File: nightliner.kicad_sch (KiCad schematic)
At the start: 81 parts, among them J1 TYPE-C-31-M-12, J2 Battery, J3 Battery, SW1 SW_SPST, SW10 SW_SPST, SW11 SW_SPST, SW12 SW_SPST, SW13 SW_SPST, SW14 SW_SPST, SW15 SW_SPST, SW16 SW_SPST, SW17 SW_SPST, SW18 SW_SPST, SW19 SW_SPST, SW2 SW_SPST, SW20 SW_SPST, SW21 ON_OFF, SW22 RESET, SW3 SW_SPST, SW4 SW_SPST, SW5 SW_SPST, SW6 SW_SPST, SW7 SW_SPST, SW8 SW_SPST, SW9 SW_SPST, U1 holyiot-18010, U2 TVS2200DRV, U3 USBLC6-2SC6, U4 BQ24075RGT, U5 XC6220B331MR

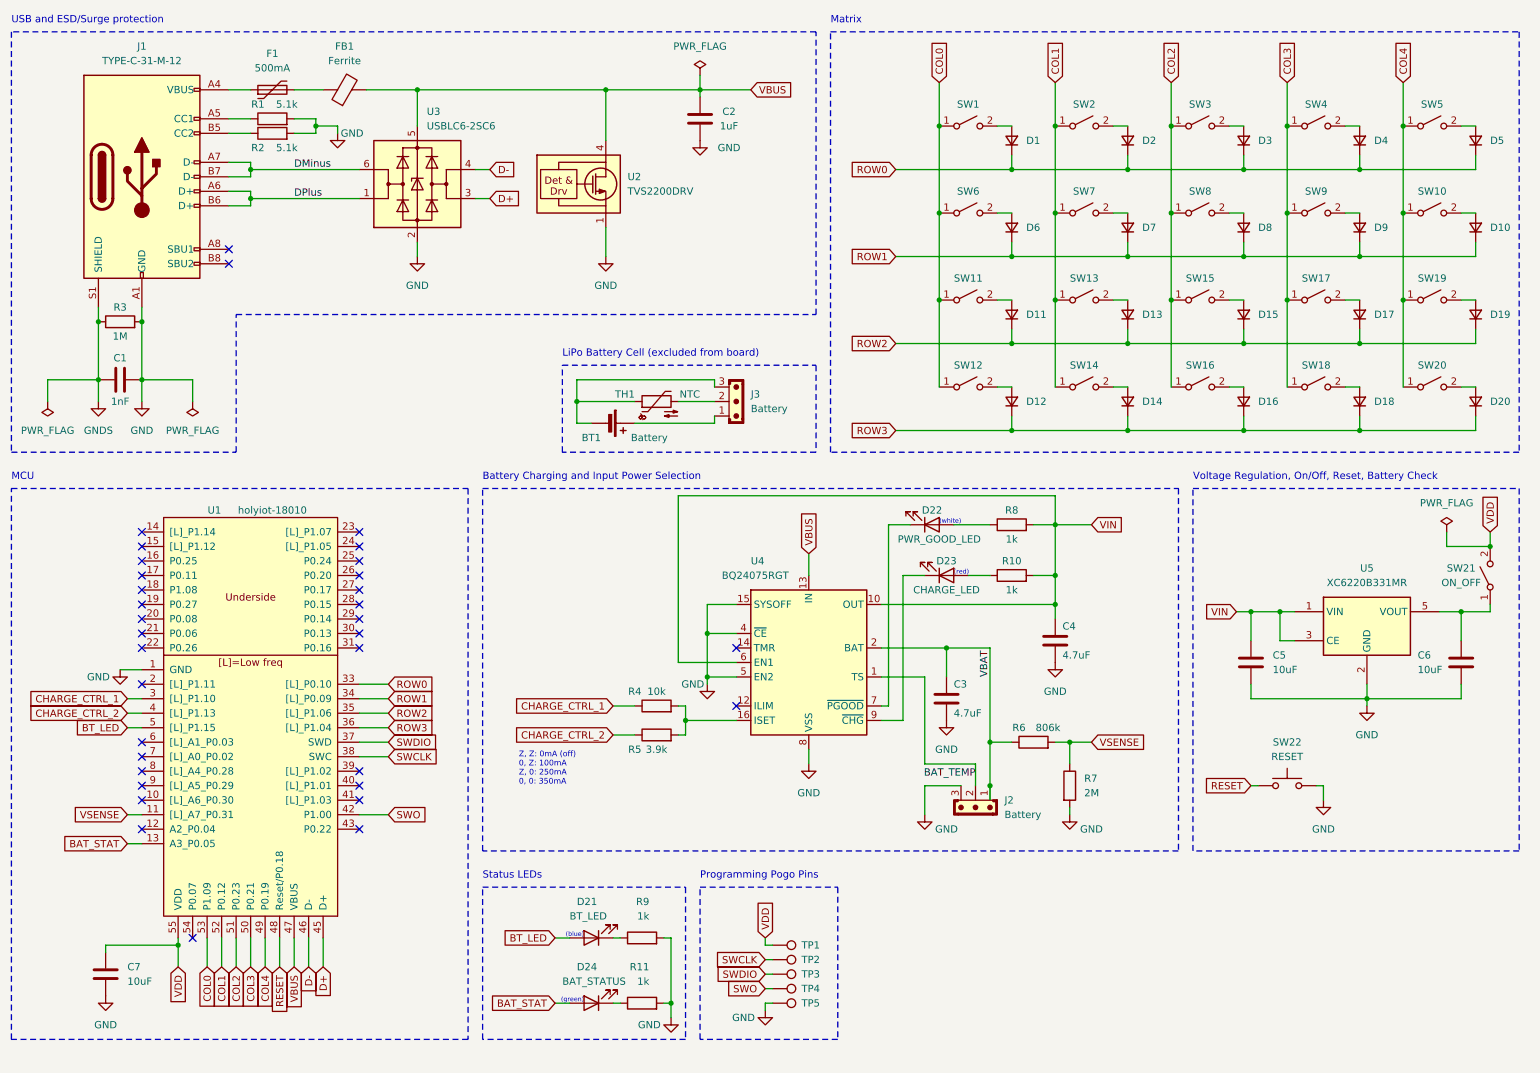
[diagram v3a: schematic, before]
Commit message: feat: routed PCB, ready for fills
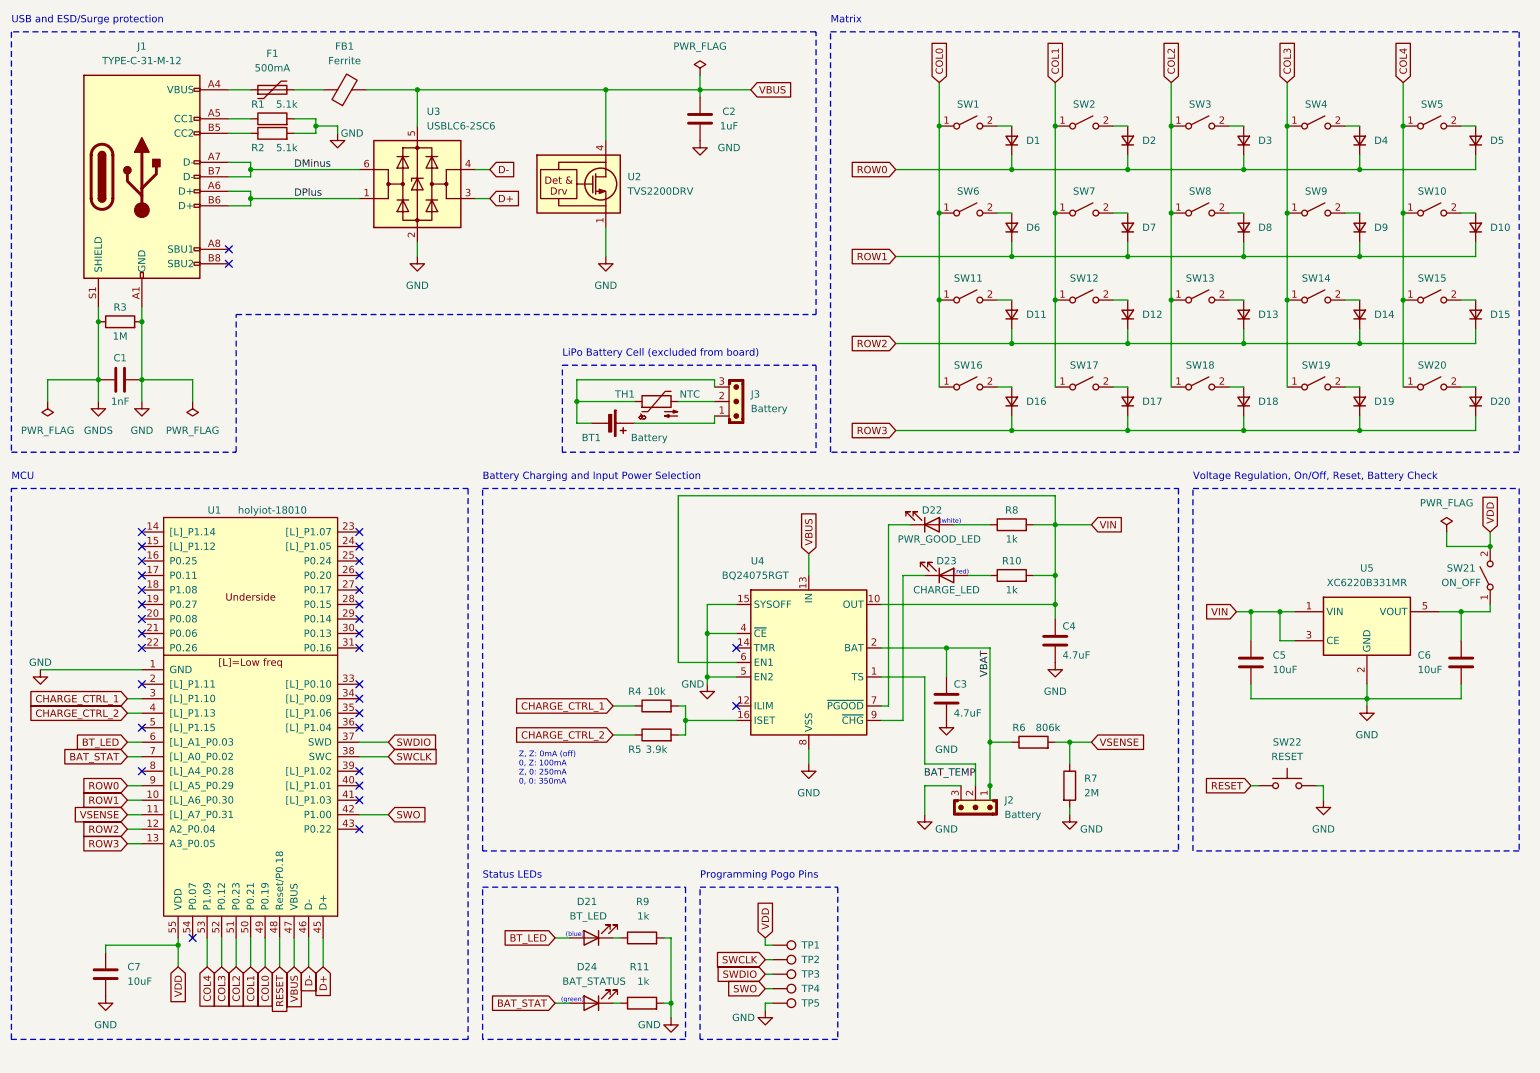
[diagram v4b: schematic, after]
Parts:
- SW1: value SW_SPST -> pinky_top
- SW10: value SW_SPST -> inner_home
- SW11: value SW_SPST -> pinky_bottom
- SW12: renamed from SW13; value SW_SPST -> ring_bottom
- SW13: renamed from SW15; value SW_SPST -> middle_bottom
- SW14: renamed from SW17; value SW_SPST -> index_bottom
- SW15: renamed from SW19; value SW_SPST -> inner_bottom
- SW16: renamed from SW12; value SW_SPST -> outer_top
- SW17: renamed from SW14; value SW_SPST -> outer_home
- SW18: renamed from SW16; value SW_SPST -> near_thumb
- SW19: renamed from SW18; value SW_SPST -> home_thumb
- SW2: value SW_SPST -> ring_top
- SW20: value SW_SPST -> far_thumb
- SW3: value SW_SPST -> middle_top
- SW4: value SW_SPST -> index_top
- SW5: value SW_SPST -> inner_top
- SW6: value SW_SPST -> pinky_home
- SW7: value SW_SPST -> ring_home
- SW8: value SW_SPST -> middle_home
- SW9: value SW_SPST -> index_home
- renumbered D13 to D12, D15 to D13, D17 to D14, D19 to D15, D12 to D16, D14 to D17, D16 to D18, D18 to D19
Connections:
- net BAT_STAT: now also U1.7 ([L]_A0_P0.02); no longer U1.13 (A3_P0.05)
- net BT_LED: now also U1.6 ([L]_A1_P0.03); no longer U1.5 ([L]_P1.15)
- net COL0: now also U1.49 (P0.19); no longer U1.53 (P1.09)
- net COL1: now also U1.50 (P0.21); no longer U1.52 (P0.12)
- net COL3: now also U1.52 (P0.12); no longer U1.50 (P0.21)
- net COL4: now also U1.53 (P1.09); no longer U1.49 (P0.19)
- net ROW0: now also U1.9 ([L]_A5_P0.29); no longer U1.33 ([L]_P0.10)
- net ROW1: now also U1.10 ([L]_A6_P0.30); no longer U1.34 ([L]_P0.09)
- net ROW2: now also U1.12 (A2_P0.04); no longer U1.35 ([L]_P1.06)
- net ROW3: now also U1.13 (A3_P0.05); no longer U1.36 ([L]_P1.04)

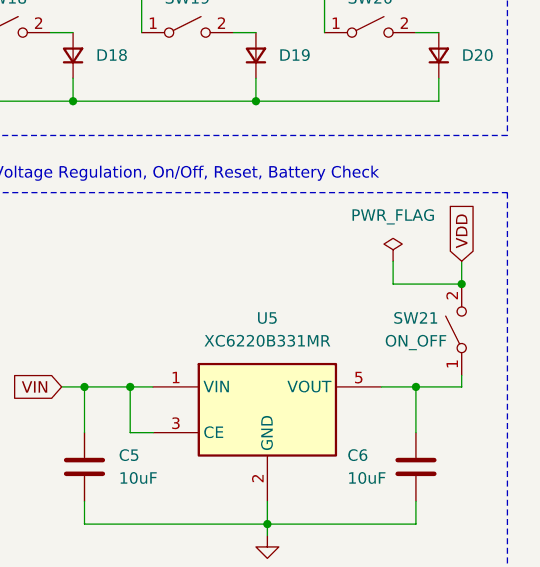
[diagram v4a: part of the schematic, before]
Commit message: fix: DRC errors, updated footprints
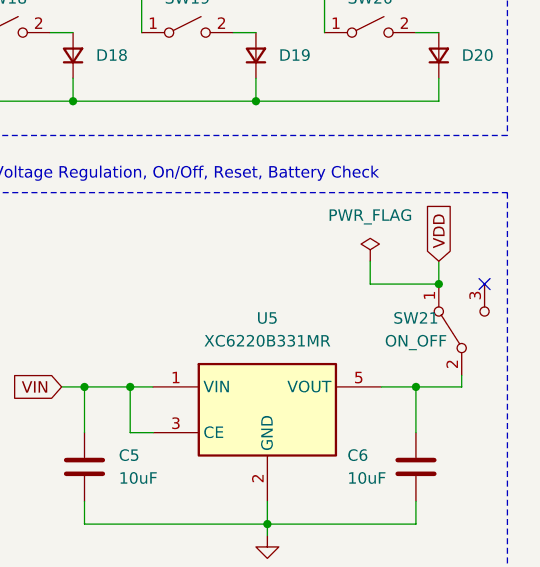
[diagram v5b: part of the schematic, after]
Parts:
- D1, D10, D11, D12, D13, D14, D15, D16, D17, D18, D19, D2, D20, D3, D4, D5, D6, D7, D8, D9: footprint keebio:D_SOD-323 -> Diode_SMD:D_SOD-323
- SW21: symbol Switch:SW_SPST -> Switch:SW_SPDT
- U4: footprint Package_DFN_QFN:VQFN-16-1EP_3x3mm_P0.5mm_EP1.6x1.6mm -> miro_keyboard:VQFN-16-1EP_3x3mm_P0.5mm_EP1.6x1.6mm_ThermalVias
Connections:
- net VDD: now also SW21.1 (A); no longer SW21.2 (B)
- net at C6.1, U5.5 (VOUT): now also SW21.2 (B); no longer SW21.1 (A)
- no-connect marks 34 -> 35
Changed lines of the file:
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@@
   (junction (at 252.73 72.39) (diameter 0) (color 0 0 0 0)
   )
-  (junction (at 275.59 107.95) (diameter 0) (color 0 0 0 0)
-  )
   (junction (at 31.75 78.74) (diameter 0) (color 0 0 0 0)
   )
@@
   (junction (at 179.07 64.77) (diameter 0) (color 0 0 0 0)
   )
+  (junction (at 273.05 107.95) (diameter 0) (color 0 0 0 0)
+  )
   (junction (at 212.09 72.39) (diameter 0) (color 0 0 0 0)
   )
@@
   (no_connect (at 77.47 118.11))
   (no_connect (at 77.47 115.57))
+  (no_connect (at 278.13 107.95))
   (no_connect (at 39.37 118.11))
   (no_connect (at 39.37 115.57))
@@
     (stroke (width 0) (type default))
   )
-  (wire (pts (xy 275.59 105.41) (xy 275.59 107.95))
+  (wire (pts (xy 273.05 105.41) (xy 273.05 107.95))
     (stroke (width 0) (type default))
   )
@@
     (stroke (width 0) (type default))
   )
-  (wire (pts (xy 267.97 107.95) (xy 275.59 107.95))
+  (wire (pts (xy 265.43 107.95) (xy 273.05 107.95))
     (stroke (width 0) (type default))
   )
@@
     (stroke (width 0) (type default))
   )
-  (wire (pts (xy 267.97 105.41) (xy 267.97 107.95))
+  (wire (pts (xy 265.43 105.41) (xy 265.43 107.95))
     (stroke (width 0) (type default))
   )
@@
     )
   )
-  (global_label "VDD" (shape input) (at 275.59 105.41 90) (fields_autoplaced)
+  (global_label "VDD" (shape input) (at 273.05 105.41 90) (fields_autoplaced)
     (effects (font (size 1.27 1.27)) (justify left))
-    (property "Intersheetrefs" "${INTERSHEET_REFS}" (at 275.59 98.7962 90)
+    (property "Intersheetrefs" "${INTERSHEET_REFS}" (at 273.05 98.7962 90)
       (effects (font (size 1.27 1.27)) (justify left) hide)
     )
@@
       (effects (font (size 1.27 1.27)) (justify right) hide)
     )
-    (property "Footprint" "keebio:D_SOD-323" (at 212.09 52.07 90)
+    (property "Footprint" "Diode_SMD:D_SOD-323" (at 212.09 52.07 90)
       (effects (font (size 1.27 1.27)) hide)
     )
@@
       (effects (font (size 1.27 1.27)) (justify right) hide)
     )
-    (property "Footprint" "keebio:D_SOD-323" (at 273.05 36.83 90)
+    (property "Footprint" "Diode_SMD:D_SOD-323" (at 273.05 36.83 90)
       (effects (font (size 1.27 1.27)) hide)
     )
@@
       (effects (font (size 1.27 1.27)) (justify right) hide)
     )
-    (property "Footprint" "keebio:D_SOD-323" (at 212.09 67.31 90)
+    (property "Footprint" "Diode_SMD:D_SOD-323" (at 212.09 67.31 90)
       (effects (font (size 1.27 1.27)) hide)
     )
@@
       (effects (font (size 1.27 1.27)) (justify right) hide)
     )
-    (property "Footprint" "keebio:D_SOD-323" (at 252.73 52.07 90)
+    (property "Footprint" "Diode_SMD:D_SOD-323" (at 252.73 52.07 90)
       (effects (font (size 1.27 1.27)) hide)
     )
@@
     )
   )
-  (symbol (lib_id "Switch:SW_SPST") (at 275.59 113.03 90) (unit 1)
+  (symbol (lib_id "Switch:SW_SPDT") (at 275.59 113.03 90) (unit 1)
     (in_bom yes) (on_board yes) (dnp no)
     (property "Reference" "SW21" (at 270.51 111.76 90)
@@
     (pin "1")
     (pin "2")
+    (pin "3")
     (instances
       (project "nightliner"
@@
     )
   )
-  (symbol (lib_id "power:PWR_FLAG") (at 267.97 105.41 0) (unit 1)
+  (symbol (lib_id "power:PWR_FLAG") (at 265.43 105.41 0) (unit 1)
     (in_bom yes) (on_board yes) (dnp no) (fields_autoplaced)
-    (property "Reference" "#FLG03" (at 267.97 103.505 0)
+    (property "Reference" "#FLG03" (at 265.43 103.505 0)
       (effects (font (size 1.27 1.27)) hide)
     )
-    (property "Value" "PWR_FLAG" (at 267.97 100.33 0)
+    (property "Value" "PWR_FLAG" (at 265.43 100.33 0)
       (effects (font (size 1.27 1.27)))
     )
-    (property "Footprint" "" (at 267.97 105.41 0)
+    (property "Footprint" "" (at 265.43 105.41 0)
       (effects (font (size 1.27 1.27)) hide)
     )
-    (property "Datasheet" "~" (at 267.97 105.41 0)
+    (property "Datasheet" "~" (at 265.43 105.41 0)
       (effects (font (size 1.27 1.27)) hide)
     )
@@
       (effects (font (size 1.27 1.27)) (justify right) hide)
     )
-    (property "Footprint" "keebio:D_SOD-323" (at 191.77 36.83 90)
+    (property "Footprint" "Diode_SMD:D_SOD-323" (at 191.77 36.83 90)
       (effects (font (size 1.27 1.27)) hide)
     )
@@
       (effects (font (size 1.27 1.27)) (justify right) hide)
     )
-    (property "Footprint" "keebio:D_SOD-323" (at 232.41 52.07 90)
+    (property "Footprint" "Diode_SMD:D_SOD-323" (at 232.41 52.07 90)
       (effects (font (size 1.27 1.27)) hide)
     )
@@
       (effects (font (size 1.27 1.27)) (justify right) hide)
     )
-    (property "Footprint" "keebio:D_SOD-323" (at 273.05 67.31 90)
+    (property "Footprint" "Diode_SMD:D_SOD-323" (at 273.05 67.31 90)
       (effects (font (size 1.27 1.27)) hide)
     )
@@
       (effects (font (size 1.27 1.27)) (justify right) hide)
     )
-    (property "Footprint" "keebio:D_SOD-323" (at 232.41 82.55 90)
+    (property "Footprint" "Diode_SMD:D_SOD-323" (at 232.41 82.55 90)
       (effects (font (size 1.27 1.27)) hide)
     )
@@
       (effects (font (size 1.27 1.27)) (justify right) hide)
     )
-    (property "Footprint" "keebio:D_SOD-323" (at 273.05 82.55 90)
+    (property "Footprint" "Diode_SMD:D_SOD-323" (at 273.05 82.55 90)
       (effects (font (size 1.27 1.27)) hide)
     )
@@
       (effects (font (size 1.27 1.27)) (justify right) hide)
     )
-    (property "Footprint" "keebio:D_SOD-323" (at 252.73 36.83 90)
+    (property "Footprint" "Diode_SMD:D_SOD-323" (at 252.73 36.83 90)
       (effects (font (size 1.27 1.27)) hide)
     )
@@
       (effects (font (size 1.27 1.27)) (justify right) hide)
     )
-    (property "Footprint" "keebio:D_SOD-323" (at 191.77 82.55 90)
+    (property "Footprint" "Diode_SMD:D_SOD-323" (at 191.77 82.55 90)
       (effects (font (size 1.27 1.27)) hide)
     )
@@
       (effects (font (size 1.27 1.27)) (justify right) hide)
     )
-    (property "Footprint" "keebio:D_SOD-323" (at 273.05 52.07 90)
+    (property "Footprint" "Diode_SMD:D_SOD-323" (at 273.05 52.07 90)
       (effects (font (size 1.27 1.27)) hide)
     )
@@
       (effects (font (size 1.27 1.27)) (justify right) hide)
     )
-    (property "Footprint" "keebio:D_SOD-323" (at 191.77 52.07 90)
+    (property "Footprint" "Diode_SMD:D_SOD-323" (at 191.77 52.07 90)
       (effects (font (size 1.27 1.27)) hide)
     )
@@
       (effects (font (size 1.27 1.27)) (justify right) hide)
     )
-    (property "Footprint" "keebio:D_SOD-323" (at 191.77 67.31 90)
+    (property "Footprint" "Diode_SMD:D_SOD-323" (at 191.77 67.31 90)
       (effects (font (size 1.27 1.27)) hide)
     )
@@
       (effects (font (size 1.27 1.27)) (justify right) hide)
     )
-    (property "Footprint" "keebio:D_SOD-323" (at 232.41 36.83 90)
+    (property "Footprint" "Diode_SMD:D_SOD-323" (at 232.41 36.83 90)
       (effects (font (size 1.27 1.27)) hide)
     )
@@
       (effects (font (size 1.27 1.27)) (justify right) hide)
     )
-    (property "Footprint" "keebio:D_SOD-323" (at 212.09 82.55 90)
+    (property "Footprint" "Diode_SMD:D_SOD-323" (at 212.09 82.55 90)
       (effects (font (size 1.27 1.27)) hide)
     )
@@
       (effects (font (size 1.27 1.27)) (justify right) hide)
     )
-    (property "Footprint" "keebio:D_SOD-323" (at 252.73 82.55 90)
+    (property "Footprint" "Diode_SMD:D_SOD-323" (at 252.73 82.55 90)
       (effects (font (size 1.27 1.27)) hide)
     )
@@
       (effects (font (size 1.27 1.27)) (justify right) hide)
     )
-    (property "Footprint" "keebio:D_SOD-323" (at 252.73 67.31 90)
+    (property "Footprint" "Diode_SMD:D_SOD-323" (at 252.73 67.31 90)
       (effects (font (size 1.27 1.27)) hide)
     )
@@
       (effects (font (size 1.27 1.27)) (justify left))
     )
-    (property "Footprint" "Package_DFN_QFN:VQFN-16-1EP_3x3mm_P0.5mm_EP1.6x1.6mm" (at 163.83 142.24 0)
+    (property "Footprint" "miro_keyboard:VQFN-16-1EP_3x3mm_P0.5mm_EP1.6x1.6mm_ThermalVias" (at 163.83 142.24 0)
       (effects (font (size 1.27 1.27)) (justify left) hide)
     )
@@
       (effects (font (size 1.27 1.27)) hide)
     )
+    (property "PartNumber" "" (at 156.21 128.27 0)
+      (effects (font (size 1.27 1.27)) hide)
+    )
+    (property "LCSCNumber" "" (at 156.21 128.27 0)
+      (effects (font (size 1.27 1.27)) hide)
+    )
     (pin "1")
     (pin "10")
@@
       (effects (font (size 1.27 1.27)) (justify right) hide)
     )
-    (property "Footprint" "keebio:D_SOD-323" (at 232.41 67.31 90)
+    (property "Footprint" "Diode_SMD:D_SOD-323" (at 232.41 67.31 90)
       (effects (font (size 1.27 1.27)) hide)
     )
@@
       (effects (font (size 1.27 1.27)) (justify right) hide)
     )
-    (property "Footprint" "keebio:D_SOD-323" (at 212.09 36.83 90)
+    (property "Footprint" "Diode_SMD:D_SOD-323" (at 212.09 36.83 90)
       (effects (font (size 1.27 1.27)) hide)
     )
